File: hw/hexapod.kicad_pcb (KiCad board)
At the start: 2 copper layers, 70 x 63.5 mm, 76 parts, among them J1 Supply Motor, J10 Conn_01x03_Pin, J11 Conn_01x03_Pin, J12 Conn_01x03_Pin, J13 Conn_01x03_Pin, J14 Conn_01x03_Pin, J15 Conn_01x03_Pin, J16 Conn_01x03_Pin, J17 Conn_01x03_Pin, J18 Conn_01x03_Pin, J19 Conn_01x03_Pin, J20 Conn_01x03_Pin, J21 Conn_01x03_Pin, J22 Conn_01x03_Pin, J23 Conn_01x03_Pin, J24 Conn_01x03_Pin, J25 Conn_01x03_Pin, J26 Conn_01x03_Pin, J27 Conn_01x03_Pin, J28 Conn_01x03_Pin, J29 Conn_01x03_Pin, J3 Conn_01x03_Pin, J30 Conn_01x03_Pin, J31 Conn_01x03_Pin, J32 Conn_01x03_Pin, J33 Conn_01x03_Pin, J34 Conn_01x03_Pin, J35 Conn_01x06_Pin, J4 Conn_01x03_Pin, J5 Conn_01x03_Pin, J6 Conn_01x03_Pin, J7 Conn_01x03_Pin, J8 Conn_01x03_Pin, J9 Conn_01x03_Pin, Q2 AOD417, U2 PCA9685PW, U3 PCA9685PW

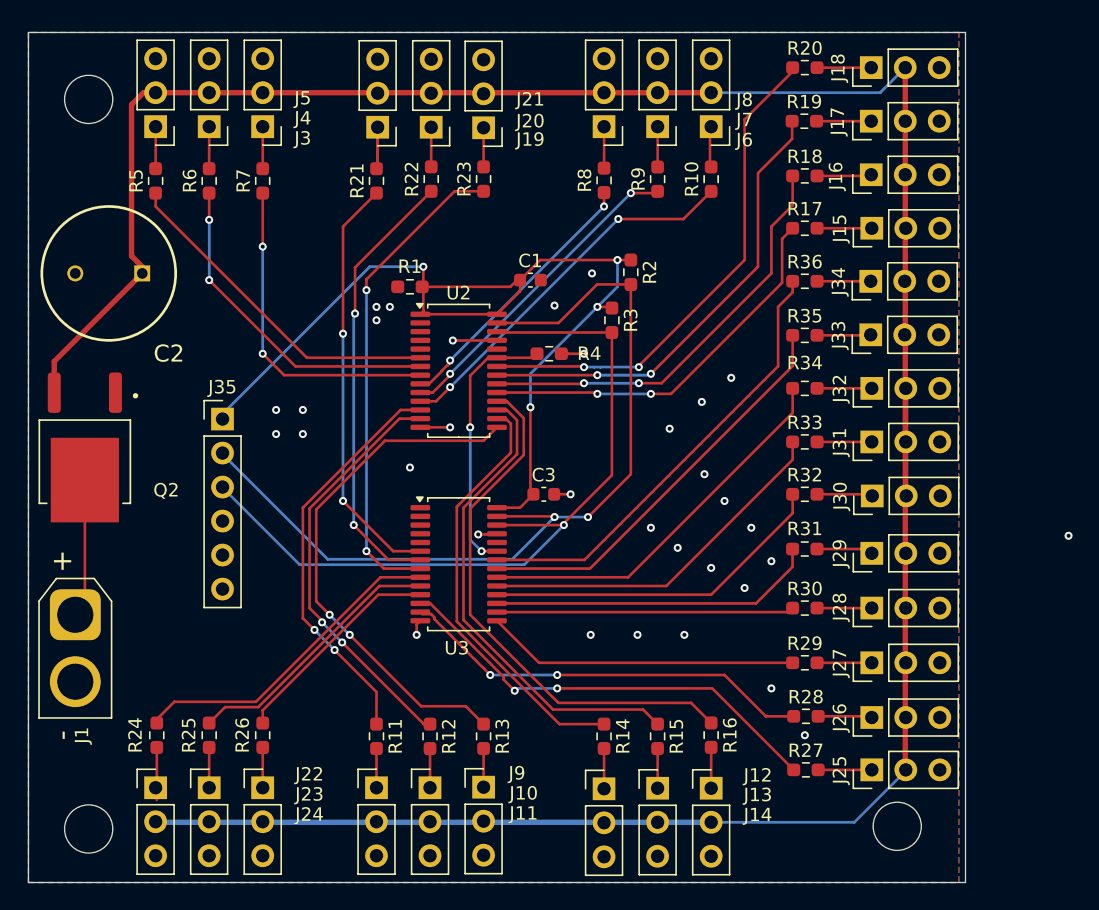
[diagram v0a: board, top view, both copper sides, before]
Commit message: hw: Keep only needed pwm
Signed-off-by: Florian Depraz <florian.depraz@outlook.com>
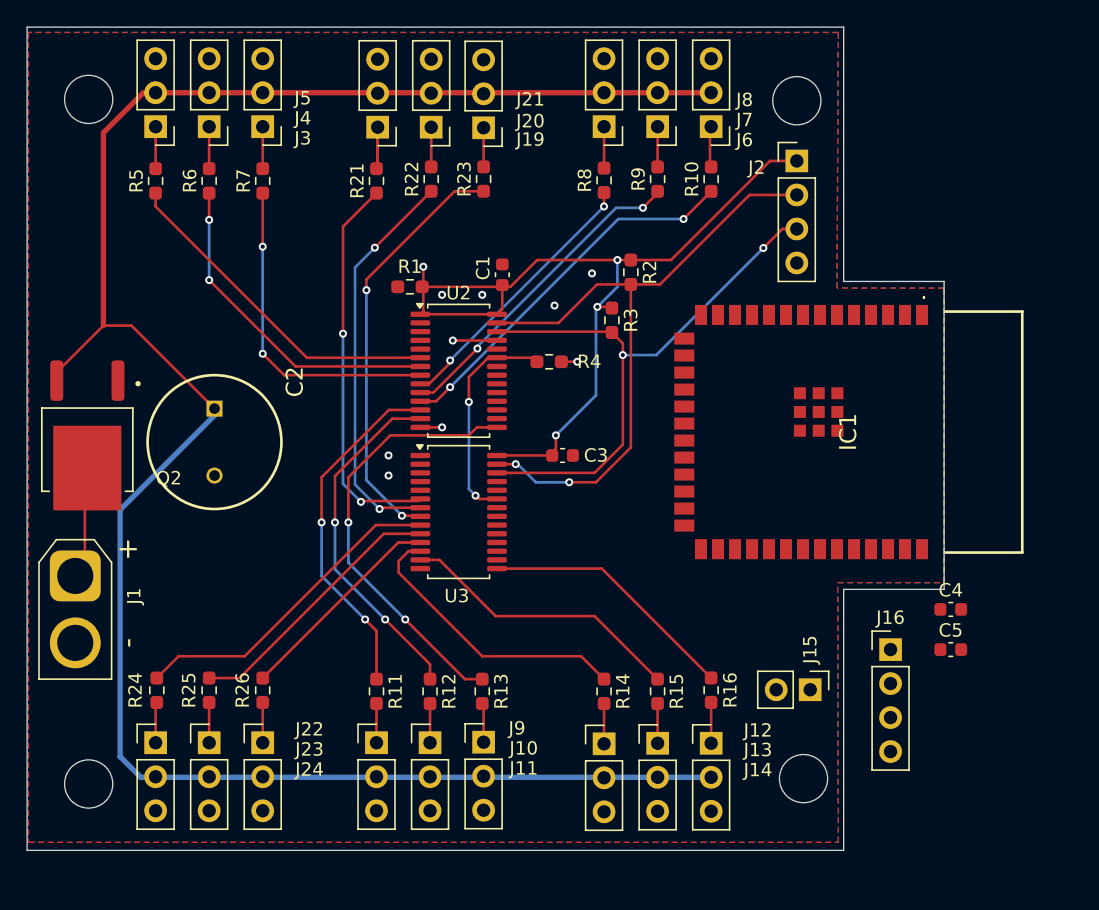
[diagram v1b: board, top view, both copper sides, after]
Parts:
- removed J17, J18, J25, J26, J27, J28, J29, J30, J31, J32, J33, J34: Conn_01x03_Pin, Connector_PinHeader_2.54mm:PinHeader_1x03_P2.54mm_Vertical
- removed J35: Conn_01x06_Pin, Connector_PinHeader_2.54mm:PinHeader_1x06_P2.54mm_Vertical
- removed R17, R18, R19, R20, R27, R28, R29, R30, R31, R32, R33, R34, R35, R36: 220, Resistor_SMD:R_0603_1608Metric_Pad0.98x0.95mm_HandSolder
- added C4: 22uF, Capacitor_SMD:C_0603_1608Metric, F.Cu at (134.4, 77.1)
- added C5: 0.1uF, Capacitor_SMD:C_0603_1608Metric, F.Cu at (134.4, 80.1)
- added IC1: ESP32-S3-WROOM-1-N8, ESP32S3WROOM1N8R2:ESP32S3WROOM1N8R2, F.Cu at (127.0, 63.9)
- added J2: Conn_01x04_Pin, Connector_PinHeader_2.54mm:PinHeader_1x04_P2.54mm_Vertical, F.Cu at (122.9, 43.6)
- J15: value Conn_01x03_Pin -> Conn_01x02_Pin; footprint Connector_PinHeader_2.54mm:PinHeader_1x03_P2.54mm_Vertical -> Connector_PinHeader_2.54mm:PinHeader_1x02_P2.54mm_Vertical
- J16: value Conn_01x03_Pin -> Conn_01x04_Pin; footprint Connector_PinHeader_2.54mm:PinHeader_1x03_P2.54mm_Vertical -> Connector_PinHeader_2.54mm:PinHeader_1x04_P2.54mm_Vertical
- moved J16 35.5 mm to (129.9, 80.1), turned to 0 degrees
- moved J15 34.8 mm to (123.9, 83.1), turned to -90 degrees
- moved C2 11.5 mm to (79.4, 62.1), turned to -90 degrees
- moved U3 3.90 mm to (97.6, 69.8)
- moved R13 3.36 mm to (99.4, 83.2)
- moved R16 3.36 mm to (116.5, 83.1)
- moved J10 3.36 mm to (95.5, 87.1)
- moved J11 3.36 mm to (99.5, 87.0)
- moved J12 3.36 mm to (108.5, 87.1)
- moved J13 3.36 mm to (112.5, 87.1)
- moved J14 3.36 mm to (116.5, 87.1)
- moved J22 3.36 mm to (75.0, 87.1)
- moved J23 3.36 mm to (79.0, 87.1)
- moved J24 3.36 mm to (83.0, 87.1)
- moved J9 3.36 mm to (91.5, 87.1)
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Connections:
- J15 pad 1: Net-(J15-Pin_1) -> GND
- J15 pad 2: +5V -> Net-(IC1-IO0)
- J16 pad 1: Net-(J16-Pin_1) -> 3V3
- J16 pad 2: +5V -> UART_TX
- J16 pad 3: GND -> UART_RX
- R14 pad 1: PWM9 -> PWM22
- R15 pad 1: PWM10 -> PWM23
- R16 pad 1: PWM11 -> PWM24
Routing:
- net +5V: track 210.2 -> 160.2 mm
- net PWM11: track 40.2 -> 0.00 mm
- net PWM15: track 37.8 -> 0.00 mm, vias 2 -> 0
- net PWM10: track 36.1 -> 0.00 mm
- net PWM14: track 34.8 -> 0.00 mm, vias 2 -> 0
- net PWM31: track 33.8 -> 0.00 mm
- net PWM13: track 31.9 -> 0.00 mm, vias 2 -> 0
- net PWM9: track 31.8 -> 0.00 mm
- net PWM30: track 30.6 -> 0.00 mm
- net PWM12: track 29.4 -> 0.00 mm, vias 2 -> 0
- net PWM29: track 29.0 -> 0.00 mm
- net PWM28: track 27.3 -> 0.07 mm
- net PWM27: track 26.0 -> 0.00 mm
- net PWM26: track 24.5 -> 0.00 mm
- net PWM25: track 22.2 -> 0.00 mm
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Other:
- board size 70 x 63.5 mm -> 68.5 x 61.5 mm

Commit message: hw: Add ESP32
Signed-off-by: Florian Depraz <florian.depraz@outlook.com>
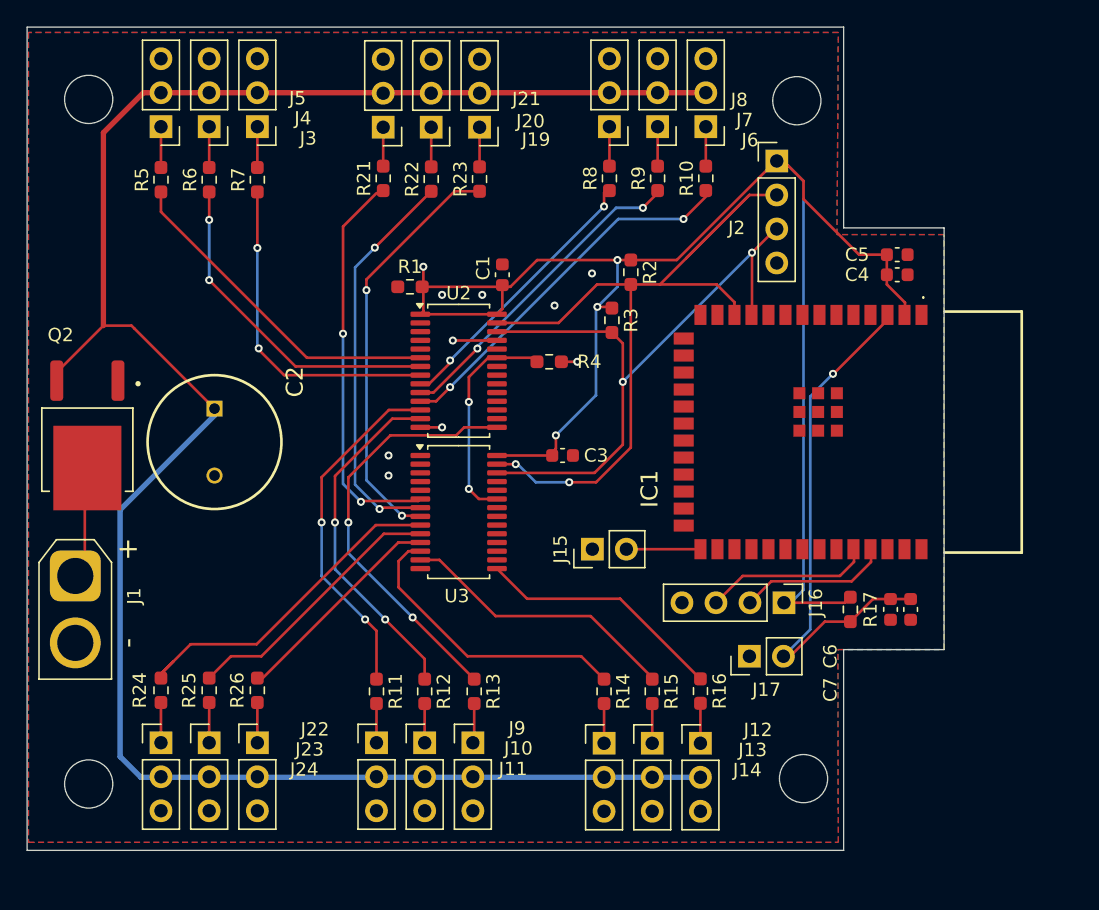
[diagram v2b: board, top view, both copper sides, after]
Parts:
- added C6: 1uF, Capacitor_SMD:C_0603_1608Metric, F.Cu at (131.4, 77.1)
- added C7: 1uF, Capacitor_SMD:C_0603_1608Metric, F.Cu at (129.9, 77.1)
- added J17: Conn_01x02_Pin, Connector_PinHeader_2.54mm:PinHeader_1x02_P2.54mm_Vertical, F.Cu at (119.4, 80.6)
- added R17: 10k, Resistor_SMD:R_0603_1608Metric_Pad0.98x0.95mm_HandSolder, F.Cu at (126.9, 77.1)
- moved C5 29.8 mm to (130.4, 50.6)
- moved C4 25.3 mm to (130.4, 52.1)
- moved J15 19.4 mm to (107.6, 72.6), turned to 90 degrees
- moved J16 8.70 mm to (121.9, 76.6), turned to -90 degrees
- moved J2 1.50 mm to (121.4, 43.6)
- moved R16 0.80 mm to (115.7, 83.2)
- moved J11 0.80 mm to (98.7, 87.1)
- moved J14 0.80 mm to (115.7, 87.1)
- moved R13 0.60 mm to (98.8, 83.2)
- moved R21 0.53 mm to (92.0, 44.9)
- moved R8 0.43 mm to (108.9, 44.9)
- moved J19 0.41 mm to (92.0, 41.1)
- moved R5 0.41 mm to (75.4, 45.0)
- moved R7 0.41 mm to (82.6, 45.0)
- moved R10 0.40 mm to (116.1, 44.9)
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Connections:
- C4 pad 1: 3V3 -> VCC
- C5 pad 1: 3V3 -> VCC
- IC1 pad 11: unconnected-(IC1-IO18-Pad11) -> SCL
- IC1 pad 12: unconnected-(IC1-IO8-Pad12) -> SDA
- IC1 pad 2: 3V3 -> VCC
- IC1 pad 3: unconnected-(IC1-EN-Pad3) -> /ESP32/NRF_EN
- J16 pad 1: 3V3 -> VCC
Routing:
- net VCC: track 65.5 -> 120.9 mm
- net /ESP32/NRF_EN: track 0.00 -> 40.0 mm, vias 0 -> 1
- net UART_RX: track 0.00 -> 13.0 mm
- net SDA: track 50.2 -> 63.0 mm
- net UART_TX: track 0.00 -> 11.8 mm
- net Net-(IC1-IO0): track 0.00 -> 5.53 mm
- net SCL: track 44.9 -> 49.4 mm
- net Net-(J19-Pin_1): track 5.96 -> 2.91 mm
- net PWM19: track 24.8 -> 26.0 mm
- net PWM8: track 32.7 -> 31.6 mm
- net +5V: track 160.2 -> 159.4 mm
- net PWM24: track 19.4 -> 18.6 mm
- net PWM22: track 21.6 -> 22.2 mm
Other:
- outline, holes or cut-outs redrawn
